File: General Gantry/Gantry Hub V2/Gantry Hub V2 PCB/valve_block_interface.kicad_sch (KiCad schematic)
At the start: 19 parts, among them J2 178-025-513R571, J6 178-025-513R571, U1 TPIC6B595N, U10 TPIC6B595N, U11 TPIC6B595N, U12 TPIC6B595N, U13 TPIC6B595N, U4 TPIC6B595N, U8 TPIC6B595N, U9 TPIC6B595N

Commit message: Finish schematic & begin layout of Hub V2
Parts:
- C10, C11, C12, C13, C14, C3, C4, C9: footprint (none) -> Capacitor_SMD:C_1206_3216Metric_Pad1.33x1.80mm_HandSolder
- R1: footprint (none) -> Resistor_SMD:R_1206_3216Metric_Pad1.30x1.75mm_HandSolder
- U1, U10, U11, U12, U13, U4, U8, U9: footprint Package_DIP:DIP-20_W7.62mm -> Package_DIP:DIP-20_W7.62mm_Socket_LongPads
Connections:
- net CHANNEL_33: now also J6.1 (A1)
- net CHANNEL_34: now also J6.2 (A2)
- net CHANNEL_35: now also J6.3 (A3)
- net CHANNEL_36: now also J6.4 (A4)
- net CHANNEL_37: now also J6.5 (A5)
- net CHANNEL_38: now also J6.6 (A6)
- net CHANNEL_39: now also J6.7 (A7)
- net CHANNEL_40: now also J6.8 (A8)
- net CHANNEL_41: now also J6.9 (A9)
- net CHANNEL_42: now also J6.10 (A10)
- net CHANNEL_43: now also J6.11 (A11)
- net CHANNEL_44: now also J6.12 (A12)
- net CHANNEL_45: now also J6.13 (A13)
- net CHANNEL_46: now also J6.14 (A14)
- net CHANNEL_47: now also J6.15 (A15)
- net CHANNEL_48: now also J6.16 (A16)
- net CHANNEL_49: now also J6.26 (B1)
- net CHANNEL_50: now also J6.27 (B2)
- net CHANNEL_51: now also J6.28 (B3)
- net CHANNEL_52: now also J6.29 (B4)
- net CHANNEL_53: now also J6.30 (B5)
- net CHANNEL_54: now also J6.31 (B6)
- net CHANNEL_55: now also J6.32 (B7)
- net CHANNEL_56: now also J6.33 (B8)
- net CHANNEL_57: now also J6.34 (B9)
- net CHANNEL_58: now also J6.35 (B10)
- net CHANNEL_59: now also J6.36 (B11)
- net CHANNEL_60: now also J6.37 (B12)
- net CHANNEL_61: now also J6.38 (B13)
- net CHANNEL_62: now also J6.39 (B14)
- net CHANNEL_63: now also J6.40 (B15)
- net CHANNEL_64: now also J6.41 (B16)
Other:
- note added: "All eight TPIC socketed in Digikey: 1175-1479-ND"

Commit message: Finalizes GH V2 part placement, about 60-75 percent done with routing
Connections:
- net CHANNEL_33: now also U13.5 (DRAIN1); no longer U10.4 (DRAIN0)
- net CHANNEL_34: now also U13.7 (DRAIN3); no longer U10.5 (DRAIN1)
- net CHANNEL_35: now also U13.14 (DRAIN4); no longer U10.6 (DRAIN2)
- net CHANNEL_36: now also U13.16 (DRAIN6); no longer U10.7 (DRAIN3)
- net CHANNEL_37: now also U12.5 (DRAIN1); no longer U10.14 (DRAIN4)
- net CHANNEL_38: now also U12.14 (DRAIN4); no longer U10.15 (DRAIN6)
- net CHANNEL_39: now also U11.5 (DRAIN1); no longer U10.16 (DRAIN6)
- net CHANNEL_40: now also U11.14 (DRAIN4); no longer U10.17 (DRAIN7)
- net CHANNEL_41: now also U11.16 (DRAIN6); no longer U11.4 (DRAIN0)
- net CHANNEL_42: now also U10.5 (DRAIN1); no longer U11.5 (DRAIN1)
- net CHANNEL_43: now also U10.7 (DRAIN3); no longer U11.6 (DRAIN2)
- net CHANNEL_44: now also U10.14 (DRAIN4); no longer U11.7 (DRAIN3)
- net CHANNEL_45: now also U10.16 (DRAIN6); no longer U11.14 (DRAIN4)
- net CHANNEL_46: now also U12.7 (DRAIN3); no longer U11.15 (DRAIN6)
- net CHANNEL_47: now also U12.16 (DRAIN6); no longer U11.16 (DRAIN6)
- net CHANNEL_48: now also U11.7 (DRAIN3); no longer U11.17 (DRAIN7)
- net CHANNEL_49: now also U13.4 (DRAIN0); no longer U12.4 (DRAIN0)
- net CHANNEL_50: now also U13.6 (DRAIN2); no longer U12.5 (DRAIN1)
- net CHANNEL_51: now also U13.15 (DRAIN6); no longer U12.6 (DRAIN2)
- net CHANNEL_52: now also U13.17 (DRAIN7); no longer U12.7 (DRAIN3)
- net CHANNEL_53: now also U12.4 (DRAIN0); no longer U12.14 (DRAIN4)
- net CHANNEL_55: now also U11.4 (DRAIN0); no longer U12.16 (DRAIN6)
- net CHANNEL_56: now also U11.15 (DRAIN6); no longer U12.17 (DRAIN7)
- net CHANNEL_57: now also U11.17 (DRAIN7); no longer U13.4 (DRAIN0)
- net CHANNEL_58: now also U10.4 (DRAIN0); no longer U13.5 (DRAIN1)
- net CHANNEL_59: now also U10.6 (DRAIN2); no longer U13.6 (DRAIN2)
- net CHANNEL_60: now also U10.15 (DRAIN6); no longer U13.7 (DRAIN3)
- net CHANNEL_61: now also U10.17 (DRAIN7); no longer U13.14 (DRAIN4)
- net CHANNEL_62: now also U12.6 (DRAIN2); no longer U13.15 (DRAIN6)
- net CHANNEL_63: now also U12.17 (DRAIN7); no longer U13.16 (DRAIN6)
- net CHANNEL_64: now also U11.6 (DRAIN2); no longer U13.17 (DRAIN7)
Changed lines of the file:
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@@
 		)
 	)
-	(label "CHANNEL_45"
+	(label "CHANNEL_40"
 		(at 99.06 130.81 0)
 		(effects
@@
 		)
 	)
-	(label "CHANNEL_47"
+	(label "CHANNEL_41"
 		(at 99.06 125.73 0)
 		(effects
@@
 		)
 	)
-	(label "CHANNEL_61"
+	(label "CHANNEL_35"
 		(at 233.68 130.81 0)
 		(effects
@@
 		)
 	)
-	(label "CHANNEL_42"
+	(label "CHANNEL_39"
 		(at 77.47 125.73 180)
 		(effects
@@
 		)
 	)
-	(label "CHANNEL_39"
+	(label "CHANNEL_45"
 		(at 46.99 125.73 0)
 		(effects
@@
 		)
 	)
-	(label "CHANNEL_49"
+	(label "CHANNEL_53"
 		(at 160.02 123.19 180)
 		(effects
@@
 		)
 	)
-	(label "CHANNEL_46"
+	(label "CHANNEL_56"
 		(at 99.06 128.27 0)
 		(effects
@@
 		)
 	)
-	(label "CHANNEL_48"
+	(label "CHANNEL_57"
 		(at 99.06 123.19 0)
 		(effects
@@
 		)
 	)
-	(label "CHANNEL_58"
+	(label "CHANNEL_33"
 		(at 212.09 125.73 180)
 		(effects
@@
 		)
 	)
-	(label "CHANNEL_51"
+	(label "CHANNEL_62"
 		(at 160.02 128.27 180)
 		(effects
@@
 		)
 	)
-	(label "CHANNEL_60"
+	(label "CHANNEL_34"
 		(at 212.09 130.81 180)
 		(effects
@@
 		)
 	)
-	(label "CHANNEL_55"
+	(label "CHANNEL_47"
 		(at 181.61 125.73 0)
 		(effects
@@
 		)
 	)
-	(label "CHANNEL_62"
+	(label "CHANNEL_51"
 		(at 233.68 128.27 0)
 		(effects
@@
 		)
 	)
-	(label "CHANNEL_41"
+	(label "CHANNEL_55"
 		(at 77.47 123.19 180)
 		(effects
@@
 		)
 	)
-	(label "CHANNEL_53"
+	(label "CHANNEL_38"
 		(at 181.61 130.81 0)
 		(effects
@@
 		)
 	)
-	(label "CHANNEL_64"
+	(label "CHANNEL_52"
 		(at 233.68 123.19 0)
 		(effects
@@
 		)
 	)
-	(label "CHANNEL_40"
+	(label "CHANNEL_61"
 		(at 46.99 123.19 0)
 		(effects
@@
 		)
 	)
-	(label "CHANNEL_33"
+	(label "CHANNEL_58"
 		(at 25.4 123.19 180)
 		(effects
@@
 		)
 	)
-	(label "CHANNEL_59"
+	(label "CHANNEL_50"
 		(at 212.09 128.27 180)
 		(effects
@@
 		)
 	)
-	(label "CHANNEL_50"
+	(label "CHANNEL_37"
 		(at 160.02 125.73 180)
 		(effects
@@
 		)
 	)
-	(label "CHANNEL_36"
+	(label "CHANNEL_43"
 		(at 25.4 130.81 180)
 		(effects
@@
 		)
 	)
-	(label "CHANNEL_43"
+	(label "CHANNEL_64"
 		(at 77.47 128.27 180)
 		(effects
@@
 		)
 	)
-	(label "CHANNEL_35"
+	(label "CHANNEL_59"
 		(at 25.4 128.27 180)
 		(effects
@@
 		)
 	)
-	(label "CHANNEL_57"
+	(label "CHANNEL_49"
 		(at 212.09 123.19 180)
 		(effects
@@
 		)
 	)
-	(label "CHANNEL_52"
+	(label "CHANNEL_46"
 		(at 160.02 130.81 180)
 		(effects
@@
 		)
 	)
-	(label "CHANNEL_37"
+	(label "CHANNEL_44"
 		(at 46.99 130.81 0)
 		(effects
@@
 		)
 	)
-	(label "CHANNEL_34"
+	(label "CHANNEL_42"
 		(at 25.4 125.73 180)
 		(effects
@@
 		)
 	)
-	(label "CHANNEL_63"
+	(label "CHANNEL_36"
 		(at 233.68 125.73 0)
 		(effects
@@
 		)
 	)
-	(label "CHANNEL_44"
+	(label "CHANNEL_48"
 		(at 77.47 130.81 180)
 		(effects
@@
 		)
 	)
-	(label "CHANNEL_56"
+	(label "CHANNEL_63"
 		(at 181.61 123.19 0)
 		(effects
@@
 		)
 	)
-	(label "CHANNEL_38"
+	(label "CHANNEL_60"
 		(at 46.99 128.27 0)
 		(effects

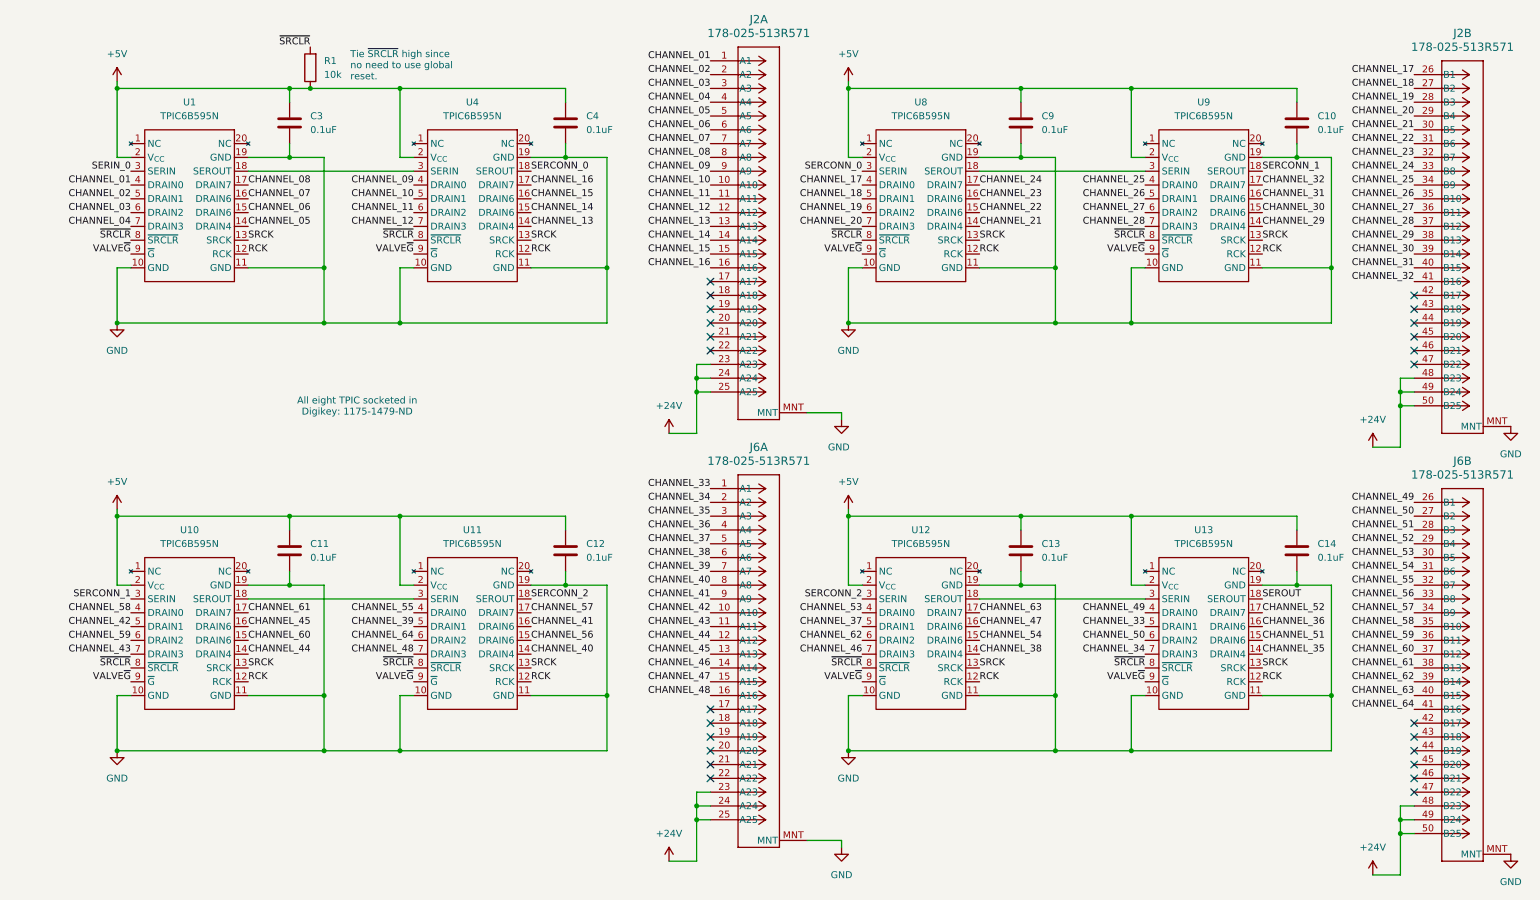
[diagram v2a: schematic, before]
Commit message: Finishes V2.0 of gantry hub box
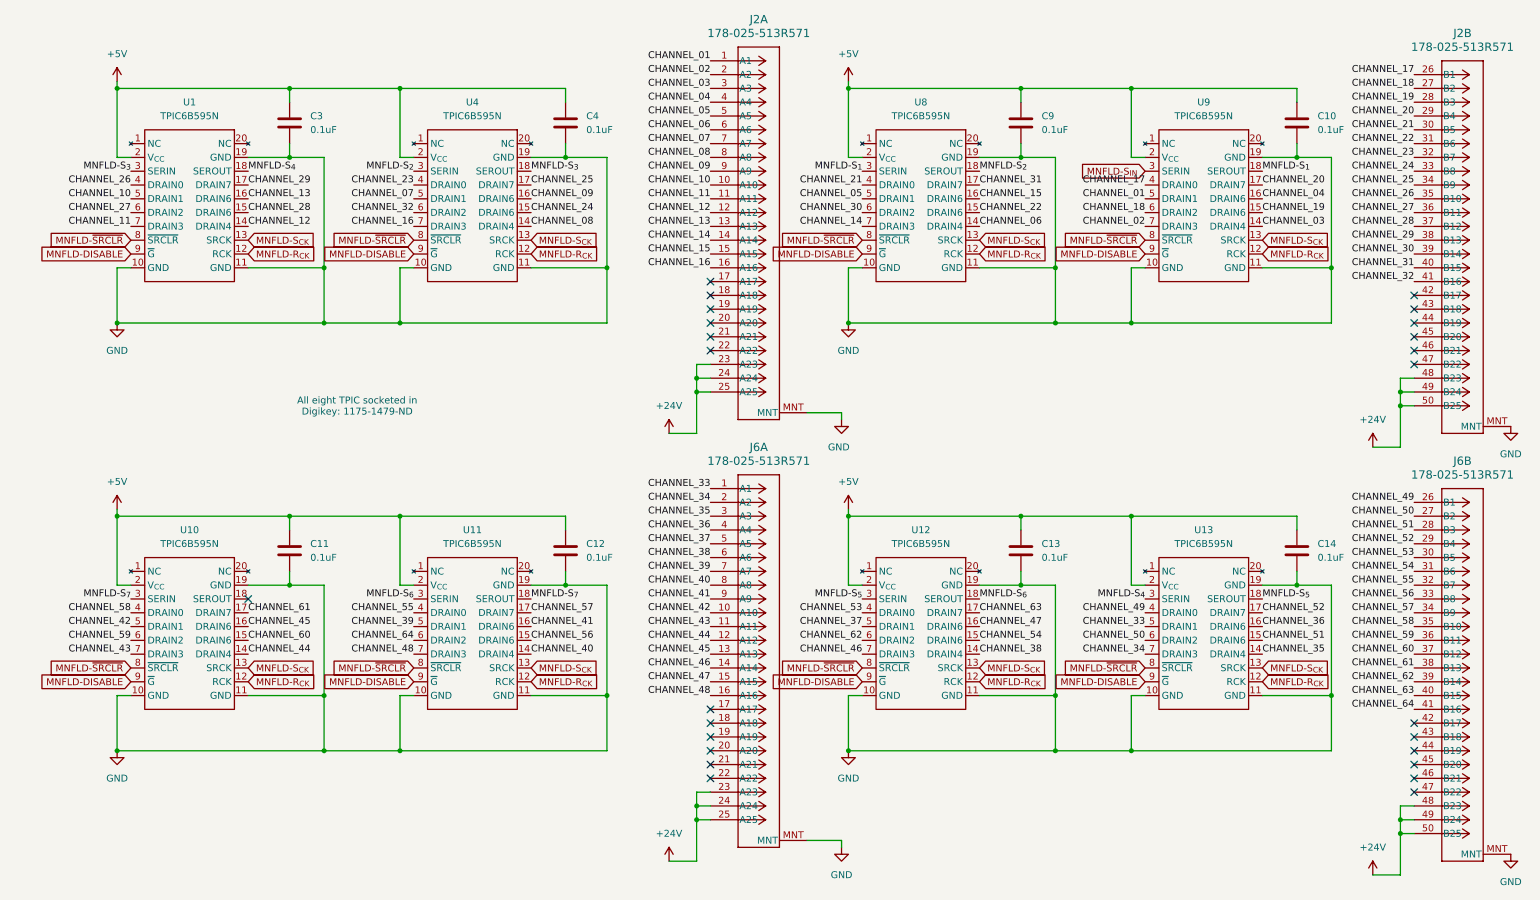
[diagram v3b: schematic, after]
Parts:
- removed R1: 10k, Resistor_SMD:R_1206_3216Metric_Pad1.30x1.75mm_HandSolder, symbol Device:R
- C10, C11, C12, C13, C14, C3, C4, C9: Digikey (none) -> 311-1179-1-ND
- J2, J6: Digikey (none) -> 1125FFE-ND
- U1, U10, U11, U12, U13, U4, U8, U9: Digikey (none) -> 296-1956-5-ND
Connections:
- net SEROUT is gone; now on net MNFLD-S_{5}: U13.18 (SEROUT)
- net CHANNEL_01: now also U9.5 (DRAIN1); no longer U1.4 (DRAIN0)
- net CHANNEL_02: now also U9.7 (DRAIN3); no longer U1.5 (DRAIN1)
- net CHANNEL_03: now also U9.14 (DRAIN4); no longer U1.6 (DRAIN2)
- net CHANNEL_04: now also U9.16 (DRAIN6); no longer U1.7 (DRAIN3)
- net CHANNEL_05: now also U8.5 (DRAIN1); no longer U1.14 (DRAIN4)
- net CHANNEL_06: now also U8.14 (DRAIN4); no longer U1.15 (DRAIN6)
- net CHANNEL_07: now also U4.5 (DRAIN1); no longer U1.16 (DRAIN6)
- net CHANNEL_08: now also U4.14 (DRAIN4); no longer U1.17 (DRAIN7)
- net CHANNEL_09: now also U4.16 (DRAIN6); no longer U4.4 (DRAIN0)
- net CHANNEL_10: now also U1.5 (DRAIN1); no longer U4.5 (DRAIN1)
- net CHANNEL_11: now also U1.7 (DRAIN3); no longer U4.6 (DRAIN2)
- net CHANNEL_12: now also U1.14 (DRAIN4); no longer U4.7 (DRAIN3)
- net CHANNEL_13: now also U1.16 (DRAIN6); no longer U4.14 (DRAIN4)
- net CHANNEL_14: now also U8.7 (DRAIN3); no longer U4.15 (DRAIN6)
- net CHANNEL_15: now also U8.16 (DRAIN6); no longer U4.16 (DRAIN6)
- net CHANNEL_16: now also U4.7 (DRAIN3); no longer U4.17 (DRAIN7)
- net CHANNEL_17: now also U9.4 (DRAIN0); no longer U8.4 (DRAIN0)
- net CHANNEL_18: now also U9.6 (DRAIN2); no longer U8.5 (DRAIN1)
- net CHANNEL_19: now also U9.15 (DRAIN6); no longer U8.6 (DRAIN2)
- net CHANNEL_20: now also U9.17 (DRAIN7); no longer U8.7 (DRAIN3)
- net CHANNEL_21: now also U8.4 (DRAIN0); no longer U8.14 (DRAIN4)
- net CHANNEL_23: now also U4.4 (DRAIN0); no longer U8.16 (DRAIN6)
- net CHANNEL_24: now also U4.15 (DRAIN6); no longer U8.17 (DRAIN7)
- net CHANNEL_25: now also U4.17 (DRAIN7); no longer U9.4 (DRAIN0)
- net CHANNEL_26: now also U1.4 (DRAIN0); no longer U9.5 (DRAIN1)
- net CHANNEL_27: now also U1.6 (DRAIN2); no longer U9.6 (DRAIN2)
- net CHANNEL_28: now also U1.15 (DRAIN6); no longer U9.7 (DRAIN3)
- net CHANNEL_29: now also U1.17 (DRAIN7); no longer U9.14 (DRAIN4)
- net CHANNEL_30: now also U8.6 (DRAIN2); no longer U9.15 (DRAIN6)
- net CHANNEL_31: now also U8.17 (DRAIN7); no longer U9.16 (DRAIN6)
- net CHANNEL_32: now also U4.6 (DRAIN2); no longer U9.17 (DRAIN7)
- net at U10.18 (SEROUT): no longer U11.3 (SERIN)
- net MNFLD-S_{2}: now reaches U8.18 (SEROUT)
- net MNFLD-S_{2}: now also U4.3 (SERIN); no longer U9.3 (SERIN)
- net MNFLD-S_{4}: now reaches U13.3 (SERIN)
- net MNFLD-S_{4}: now also U1.18 (SEROUT); no longer U12.18 (SEROUT)
- net RCK renamed MNFLD-R_{CK}
- net SERCONN_0 renamed MNFLD-S_{1}
- net MNFLD-S_{1}: now also U9.18 (SEROUT); no longer U4.18 (SEROUT)
- net SERCONN_1 renamed MNFLD-S_{7}
- net MNFLD-S_{7}: now also U11.18 (SEROUT); no longer U9.18 (SEROUT)
- net SERCONN_2 renamed MNFLD-S_{5}
- net MNFLD-S_{5}: no longer U11.18 (SEROUT)
- net SERIN_0 renamed MNFLD-S_{3}
- net MNFLD-S_{3}: now also U4.18 (SEROUT)
- net SRCK renamed MNFLD-S_{CK}
- net VALVE~{G} renamed MNFLD-DISABLE
- net ~{SRCLR} renamed MNFLD-~{SRCLR}
- new net MNFLD-S_{6}: U11.3 (SERIN), U12.18 (SEROUT)
- new net MNFLD-S_{IN}: U9.3 (SERIN)
- no-connect marks 24 -> 25
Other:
- note removed: "Tie ~{SRCLR} high since no need to use global reset."
